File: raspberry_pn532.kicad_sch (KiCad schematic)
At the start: 1 part, among them J1 Raspberry_Pi_zero_2w

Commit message: Rename sheet to 'Raspberry' and enlarge with 3.5mm pin spacing
- Sheet size: 49.53x115.57 -> 80.0x200.0
- 26 left pins, 27 right pins, 1 top pin
- 3.5mm spacing between hierarchical pins
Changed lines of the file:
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@@
-	(wire
-		(pts
-			(xy 137.16 86.36) (xy 127 86.36)
-		)
-		(stroke
-			(width 0)
-			(type default)
-		)
-	)
 	(wire
 		(pts
@@
 	(wire
 		(pts
-			(xy 139.7 80.01) (xy 139.7 91.44)
-		)
-		(stroke
-			(width 0)
-			(type default)
-		)
-	)
-	(wire
-		(pts
 			(xy 106.68 153.67) (xy 109.22 153.67)
 		)
@@
 	(wire
 		(pts
-			(xy 139.7 91.44) (xy 127 91.44)
-		)
-		(stroke
-			(width 0)
-			(type default)
-		)
-	)
-	(wire
-		(pts
 			(xy 101.6 35.56) (xy 119.38 35.56)
 		)
@@
 	(wire
 		(pts
-			(xy 137.16 82.55) (xy 137.16 86.36)
-		)
-		(stroke
-			(width 0)
-			(type default)
-		)
-	)
-	(wire
-		(pts
 			(xy 127 139.7) (xy 128.27 139.7)
 		)
@@
 		)
 	)
-		(hierarchical_label "GPIO21/SCLK1"
+	(hierarchical_label "GPIO21/SCLK1"
 		(shape bidirectional)
 		(at 86.36 78.74 180)
@@
 		)
 	)
-		(hierarchical_label "GPIO24"
+	(hierarchical_label "GPIO24"
 		(shape bidirectional)
 		(at 86.36 88.9 180)
@@
 		)
 	)
-		(hierarchical_label "SD_"
+	(hierarchical_label "SD_"
 		(shape bidirectional)
 		(at 86.36 116.84 180)
@@
 		)
 	)
-		(hierarchical_label "USB_DM"
+	(hierarchical_label "USB_DM"
 		(shape bidirectional)
 		(at 127 146.05 0)
@@
 		)
 	)
-		(hierarchical_label "GCLK0/GPIO4"
+	(hierarchical_label "GCLK0/GPIO4"
 		(shape bidirectional)
 		(at 127 71.12 0)
@@
 		)
 	)
-		(hierarchical_label "STATUS_LED"
+	(hierarchical_label "STATUS_LED"
 		(shape bidirectional)
 		(at 127 132.08 0)
@@
 		)
 	)
-			(hierarchical_label "BT_ON"
+	(hierarchical_label "BT_ON"
 		(shape bidirectional)
 		(at 127 111.76 0)
@@
 		)
 	)
-		(hierarchical_label "ID_SD/GPIO0"
+	(hierarchical_label "ID_SD/GPIO0"
 		(shape bidirectional)
 		(at 127 55.88 0)
@@
 		)
 	)
-		(hierarchical_label "WL_ON"
+	(hierarchical_label "WL_ON"
 		(shape bidirectional)
 		(at 127 114.3 0)
@@
 		)
 	)
-		(hierarchical_label "USB_DP"
+	(hierarchical_label "USB_DP"
 		(shape bidirectional)
 		(at 127 143.51 0)
@@
 		)
 	)
-		(symbol
+	(symbol
 		(lib_id "Connector:Raspberry_Pi_zero_2w")
 		(at 106.68 78.74 0)

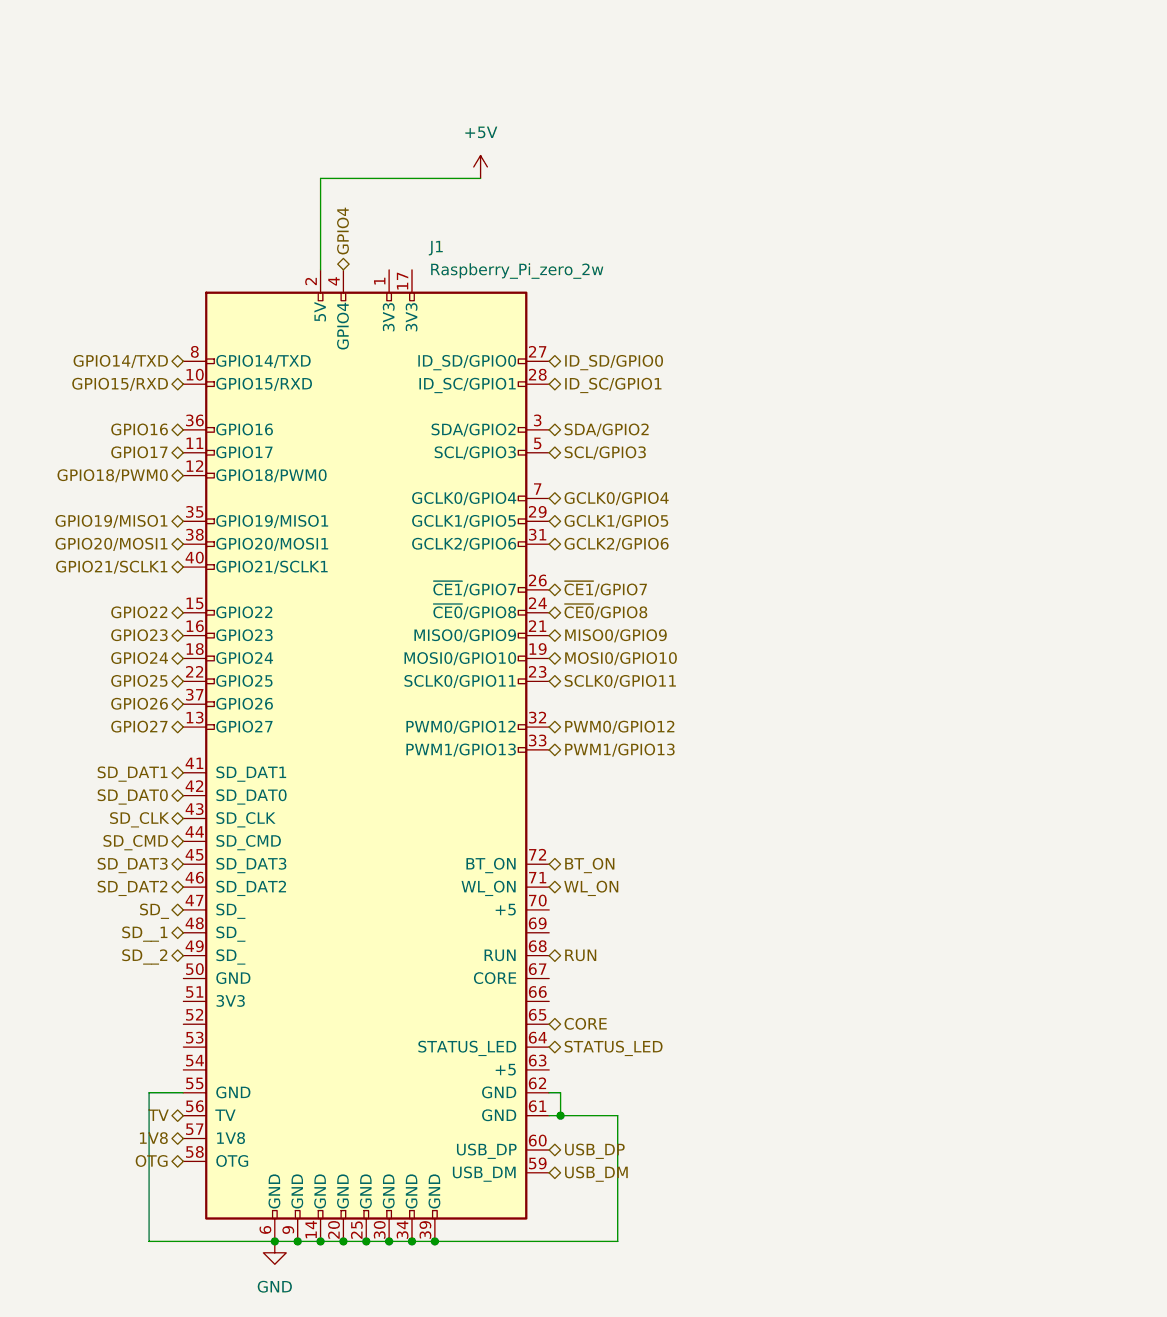
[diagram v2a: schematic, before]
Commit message: Add hierarchical labels/pins across all sheets, fix DiscoveryAnalog3 rename, PCB 99x99mm rounded corners
- nfc_rpi.kicad_sch: 19 hierarchical pins on PN532 sheet
- pn532.kicad_sch: 22 hierarchical labels with _PN532 suffix
- raspberry_pn532.kicad_sch: 68 hierarchical labels for J1
- nfc.kicad_sch: 54 signal pins on Raspberry sheet, power pins removed
- switch.kicad_sch: 8 switch+resistor circuits with hierarchical labels
- oled.kicad_sch: 7 hierarchical labels
- DiscoveryAnalog3.kicad_sch: 26 hierarchical labels for J4 connector
- nfc_rpi.kicad_pcb: 99x99mm board outline with 5mm rounded corners (gr_line + gr_arc)
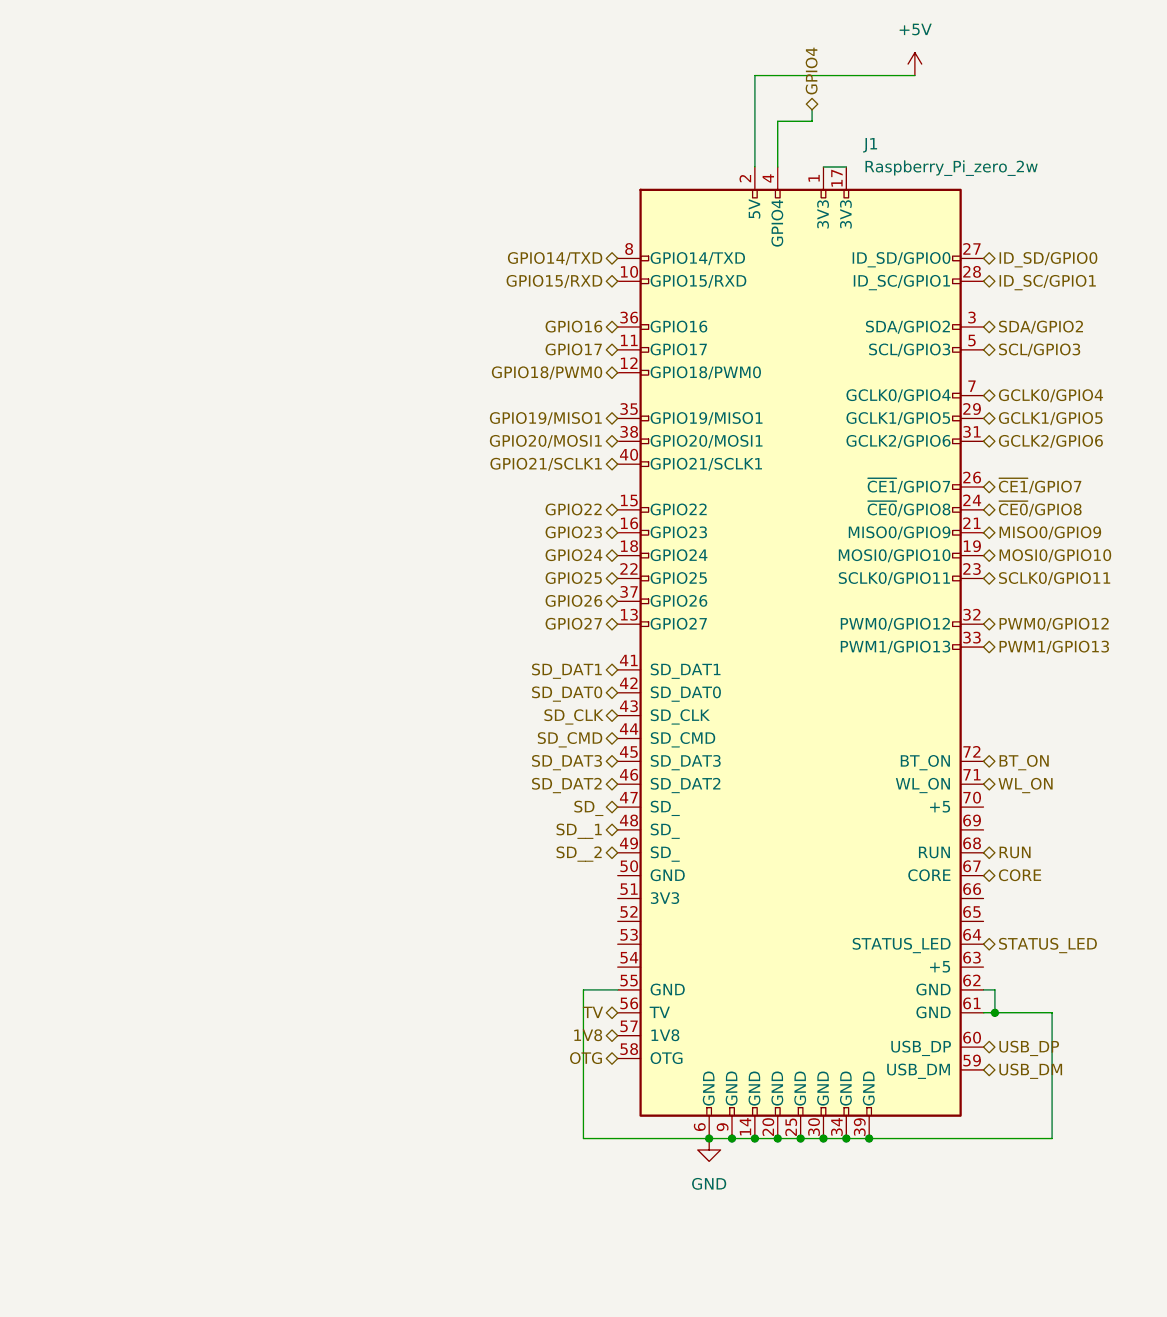
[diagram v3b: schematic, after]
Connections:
- net CORE: now also J1.67 (CORE); no longer J1.65
- net at J1.1 (3V3): now also J1.17 (3V3)
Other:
- moved on the sheet: J1
